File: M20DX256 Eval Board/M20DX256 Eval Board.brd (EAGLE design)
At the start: 60 x 30 mm, 20 parts, among them J1 M52-040000S0545, J2 20_PIN, J3 20_PIN, SW1 KMR211G, U1 MK20DX256VLH7, Y1 8MHz, Y2 32.768kHz, 12.5pF

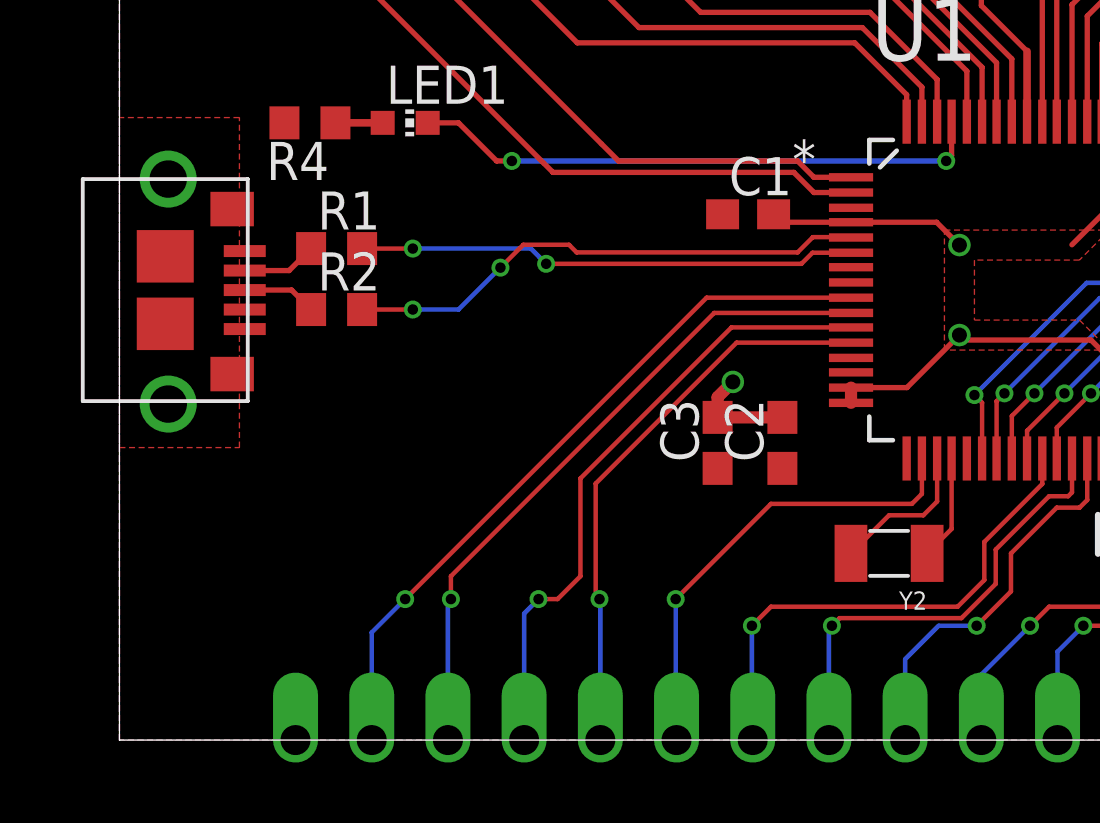
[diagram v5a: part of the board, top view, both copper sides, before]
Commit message: Add LED power to the schematic and route the board
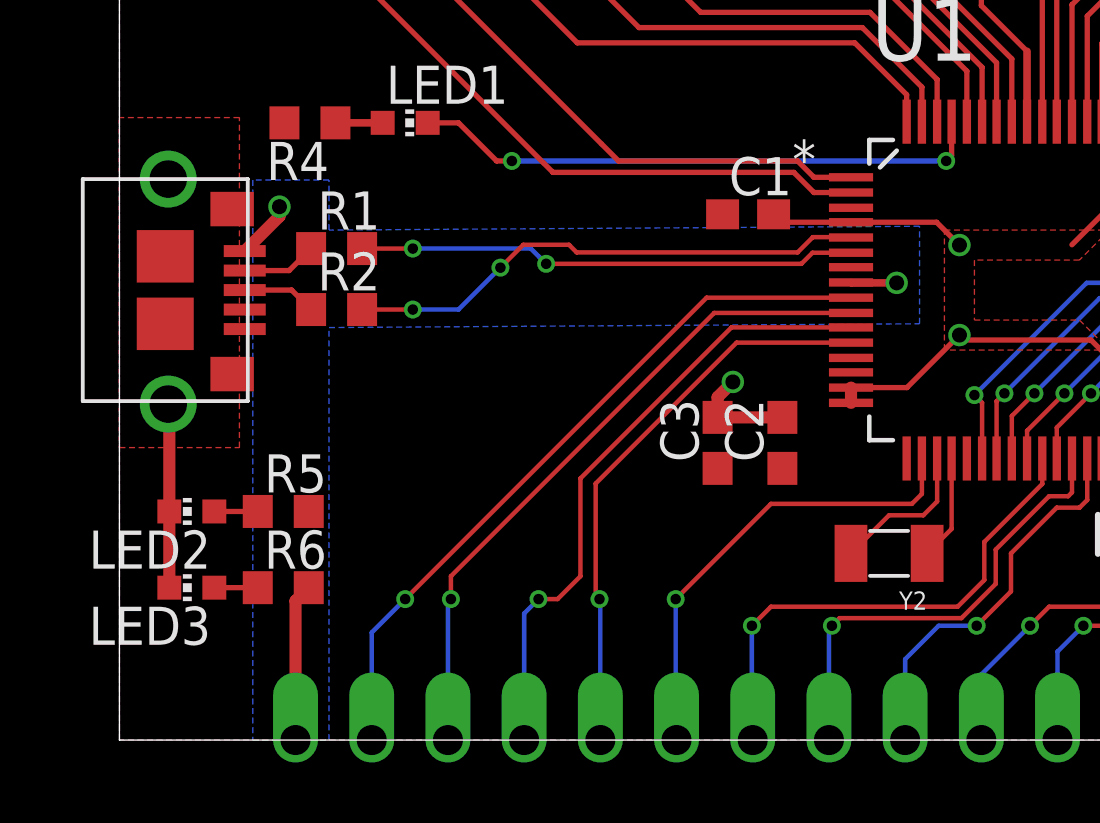
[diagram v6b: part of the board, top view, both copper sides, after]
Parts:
- added LED2, LED3: (no value), led:CHIP-LED0603
- added R5: 1k, rcl:R0603
- added R6: 1k5, rcl:R0603
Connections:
- new net N$10: LED2.A, R5.1
- new net N$9: LED3.A, R6.1
- net +3V3: now also R5.2
- net +5V: now also R6.2
- net GND: now also LED2.C, LED3.C
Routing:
- net +5V: track 0.00 -> 8.75 mm, vias 0 -> 2
- net GND: track 38.6 -> 44.8 mm
- net N$9: track 0.00 -> 1.45 mm
- net N$10: track 0.00 -> 1.45 mm
- added copper zone on layer 16, net +5V
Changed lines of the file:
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@@
 <element name="LED1" library="led" package="CHIP-LED0603" value="" x="9.525" y="20.574" rot="R270"/>
 <element name="R4" library="rcl" package="R0603" value="1k" x="6.35" y="20.574" rot="R180"/>
+<element name="R5" library="rcl" package="R0603" value="1k" x="5.461" y="7.62"/>
+<element name="R6" library="rcl" package="R0603" value="1k5" x="5.461" y="5.08"/>
+<element name="LED2" library="led" package="CHIP-LED0603" value="" x="2.413" y="7.62" rot="R90"/>
+<element name="LED3" library="led" package="CHIP-LED0603" value="" x="2.413" y="5.08" rot="R90"/>
 </elements>
 <signals>
@@
 <vertex x="0" y="0"/>
 </polygon>
+<contactref element="R5" pad="2"/>
 <wire x1="67.31" y1="26.25" x2="72.771" y2="26.123" width="0" layer="19" extent="1-1"/>
 <wire x1="57.035" y1="21.35" x2="67.31" y2="26.25" width="0" layer="19" extent="1-1"/>
@@
 <contactref element="SW1" pad="1"/>
 <contactref element="Y1" pad="2"/>
-<polygon width="0.4064" layer="16">
+<polygon width="0.4064" layer="16" rank="3">
 <vertex x="0" y="30"/>
 <vertex x="60" y="30"/>
@@
 <wire x1="37.6432" y1="18.2512" x2="38.227" y2="18.835" width="0.1778" layer="1"/>
 <contactref element="J3" pad="P$20"/>
+<contactref element="LED2" pad="C"/>
+<contactref element="LED3" pad="C"/>
+<wire x1="1.663" y1="5.08" x2="1.663" y2="7.62" width="0.4064" layer="1"/>
+<wire x1="1.663" y1="7.62" x2="1.663" y2="11.164" width="0.4064" layer="1"/>
+<wire x1="1.663" y1="11.164" x2="1.627" y2="11.2" width="0.4064" layer="1"/>
 <wire x1="67.31" y1="24.55" x2="72.771" y2="24.423" width="0" layer="19" extent="1-1"/>
 <wire x1="57.035" y1="20.08" x2="67.31" y2="24.55" width="0" layer="19" extent="1-1"/>
-<wire x1="54.13" y1="30" x2="57.035" y2="20.08" width="0" layer="19" extent="1-1"/>
 </signal>
 <signal name="+5V">
@@
 <contactref element="U1" pad="8"/>
 <contactref element="J2" pad="P$20"/>
-<wire x1="4.177" y1="16.3" x2="24.3866" y2="15.254" width="0" layer="19" extent="1-1"/>
-<wire x1="5.87" y1="0" x2="4.177" y2="16.3" width="0" layer="19" extent="1-1"/>
+<polygon width="0.1778" layer="16" spacing="0.254">
+<vertex x="4.445" y="0"/>
+<vertex x="6.985" y="0"/>
+<vertex x="6.985" y="13.75"/>
+<vertex x="26.67" y="13.877"/>
+<vertex x="26.67" y="17.127"/>
+<vertex x="6.985" y="17"/>
+<vertex x="6.985" y="18.669"/>
+<vertex x="4.445" y="18.669"/>
+</polygon>
+<wire x1="4.177" y1="16.3" x2="5.334" y2="17.457" width="0.4064" layer="1"/>
+<wire x1="5.334" y1="17.457" x2="5.334" y2="17.78" width="0.4064" layer="1"/>
+<via x="5.334" y="17.78" extent="1-16" drill="0.5"/>
+<wire x1="24.3866" y1="15.254" x2="24.4006" y2="15.24" width="0.254" layer="1"/>
+<wire x1="24.4006" y1="15.24" x2="25.908" y2="15.24" width="0.254" layer="1"/>
+<via x="25.908" y="15.24" extent="1-16" drill="0.5"/>
+<contactref element="R6" pad="2"/>
+<wire x1="5.87" y1="0" x2="5.87" y2="4.639" width="0.4064" layer="1"/>
+<wire x1="5.87" y1="4.639" x2="6.311" y2="5.08" width="0.4064" layer="1"/>
 </signal>
 <signal name="N$1">
@@
 <wire x1="18.542" y1="0.028" x2="18.57" y2="0" width="0.15" layer="16"/>
 </signal>
+<signal name="N$9">
+<contactref element="LED3" pad="A"/>
+<contactref element="R6" pad="1"/>
+<wire x1="4.611" y1="5.08" x2="3.163" y2="5.08" width="0.1778" layer="1"/>
+</signal>
+<signal name="N$10">
+<contactref element="LED2" pad="A"/>
+<contactref element="R5" pad="1"/>
+<wire x1="4.611" y1="7.62" x2="3.163" y2="7.62" width="0.1778" layer="1"/>
+</signal>
 </signals>

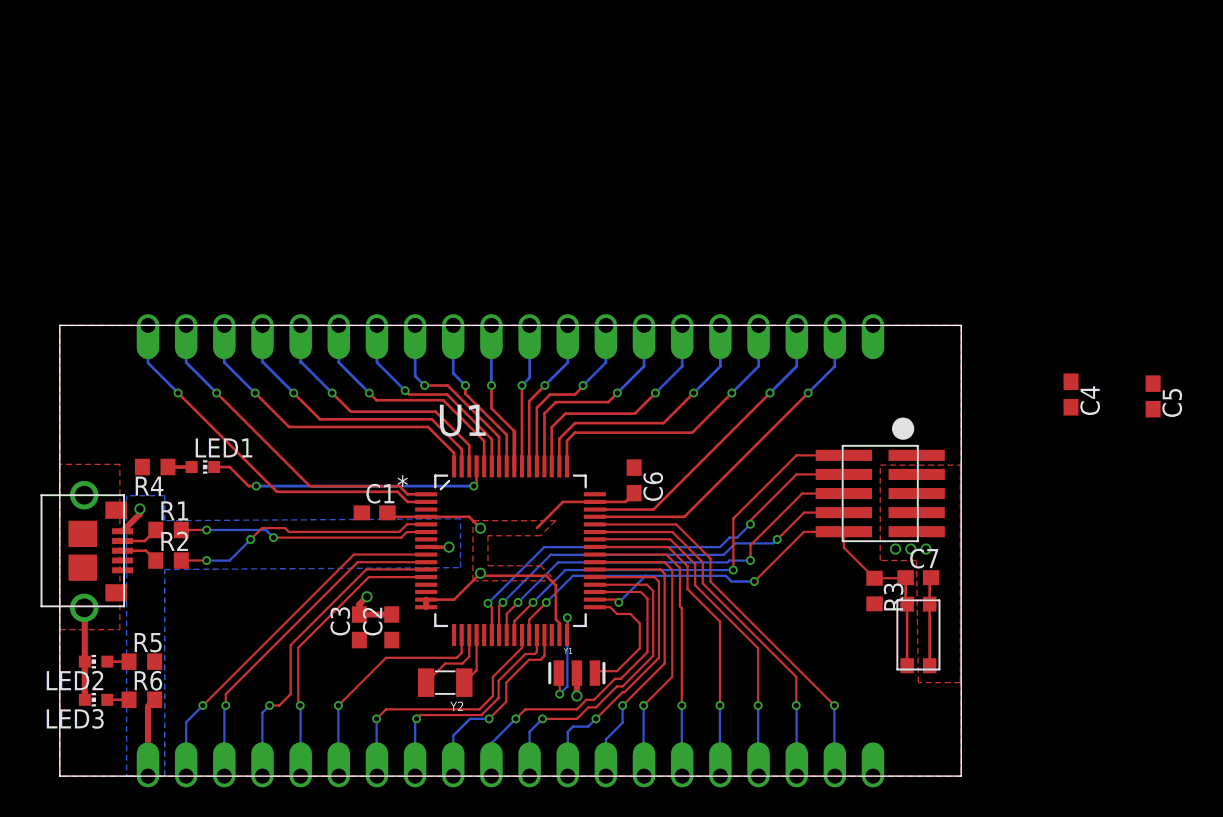
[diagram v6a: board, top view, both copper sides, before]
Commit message: Add test pad and curve the corner of the board
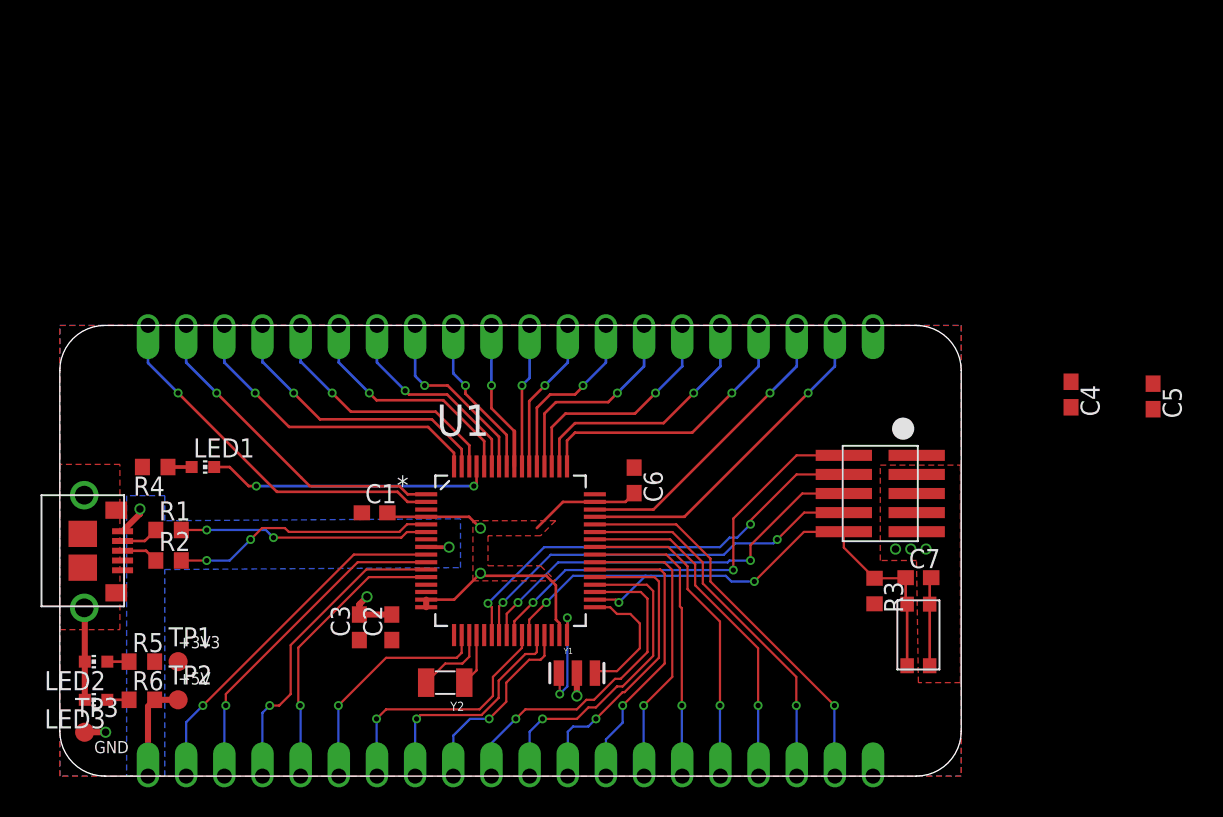
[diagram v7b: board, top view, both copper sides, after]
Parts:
- added TP1, TP2, TP3: TPB1,27, testpad:B1,27
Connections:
- net +3V3: now also TP1.TP
- net +5V: now also TP2.TP
- net GND: now also TP3.TP
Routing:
- net +5V: track 8.75 -> 10.3 mm
- net GND: track 44.8 -> 46.2 mm, vias 7 -> 8
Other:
- outline, holes or cut-outs redrawn
- board text added: "+3V3"
- board text added: "+5V"
- board text added: "GND"
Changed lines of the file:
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@@
 <layer number="46" name="Milling" color="3" fill="1" visible="no" active="yes"/>
 <layer number="47" name="Measures" color="7" fill="1" visible="no" active="yes"/>
-<layer number="48" name="Document" color="7" fill="1" visible="no" active="yes"/>
+<layer number="48" name="Document" color="7" fill="1" visible="yes" active="yes"/>
 <layer number="49" name="Reference" color="7" fill="1" visible="no" active="yes"/>
 <layer number="50" name="dxf" color="7" fill="1" visible="no" active="no"/>
@@
 <board>
 <plain>
-<wire x1="0" y1="0" x2="60" y2="0" width="0" layer="20"/>
-<wire x1="60" y1="0" x2="60" y2="30" width="0" layer="20"/>
-<wire x1="60" y1="30" x2="0" y2="30" width="0" layer="20"/>
-<wire x1="0" y1="30" x2="0" y2="0" width="0" layer="20"/>
+<wire x1="57" y1="30" x2="3" y2="30" width="0" layer="20"/>
+<wire x1="3" y1="30" x2="0" y2="27" width="0" layer="20" curve="90"/>
+<wire x1="0" y1="27" x2="0" y2="3" width="0" layer="20"/>
+<wire x1="0" y1="3" x2="3" y2="0" width="0" layer="20" curve="90"/>
+<wire x1="3" y1="0" x2="57" y2="0" width="0" layer="20"/>
+<wire x1="57" y1="0" x2="60" y2="3" width="0" layer="20" curve="90"/>
+<wire x1="60" y1="3" x2="60" y2="27" width="0" layer="20"/>
+<wire x1="60" y1="27" x2="57" y2="30" width="0" layer="20" curve="90"/>
+<text x="7.874" y="8.509" size="0.8128" layer="21">+3V3</text>
+<text x="7.874" y="6.096" size="0.8128" layer="21">+5V</text>
+<text x="2.286" y="1.524" size="0.8128" layer="21">GND</text>
 </plain>
 <attributes>
@@
 <element name="LED2" library="led" package="CHIP-LED0603" value="" x="2.413" y="7.62" rot="R90"/>
 <element name="LED3" library="led" package="CHIP-LED0603" value="" x="2.413" y="5.08" rot="R90"/>
+<element name="TP1" library="testpad" package="B1,27" value="TPB1,27" x="7.874" y="7.62">
+<attribute name="TP_SIGNAL_NAME" value="" x="7.874" y="7.62" size="1.778" layer="27" display="off"/>
+</element>
+<element name="TP2" library="testpad" package="B1,27" value="TPB1,27" x="7.874" y="5.08">
+<attribute name="TP_SIGNAL_NAME" value="" x="7.874" y="5.08" size="1.778" layer="27" display="off"/>
+</element>
+<element name="TP3" library="testpad" package="B1,27" value="TPB1,27" x="1.651" y="2.921">
+<attribute name="TP_SIGNAL_NAME" value="" x="1.651" y="2.921" size="0.8128" layer="27" display="off"/>
+</element>
 </elements>
 <signals>
@@
 </polygon>
 <contactref element="R5" pad="2"/>
+<contactref element="TP1" pad="TP"/>
 <wire x1="67.31" y1="26.25" x2="72.771" y2="26.123" width="0" layer="19" extent="1-1"/>
 <wire x1="57.035" y1="21.35" x2="67.31" y2="26.25" width="0" layer="19" extent="1-1"/>
@@
 <wire x1="1.663" y1="7.62" x2="1.663" y2="11.164" width="0.4064" layer="1"/>
 <wire x1="1.663" y1="11.164" x2="1.627" y2="11.2" width="0.4064" layer="1"/>
+<contactref element="TP3" pad="TP"/>
+<via x="3.048" y="2.921" extent="1-16" drill="0.5"/>
+<wire x1="1.651" y1="2.921" x2="3.048" y2="2.921" width="0.4064" layer="1"/>
 <wire x1="67.31" y1="24.55" x2="72.771" y2="24.423" width="0" layer="19" extent="1-1"/>
 <wire x1="57.035" y1="20.08" x2="67.31" y2="24.55" width="0" layer="19" extent="1-1"/>
@@
 <wire x1="5.87" y1="0" x2="5.87" y2="4.639" width="0.4064" layer="1"/>
 <wire x1="5.87" y1="4.639" x2="6.311" y2="5.08" width="0.4064" layer="1"/>
+<contactref element="TP2" pad="TP"/>
+<wire x1="6.311" y1="5.08" x2="7.874" y2="5.08" width="0.4064" layer="1"/>
 </signal>
 <signal name="N$1">

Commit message: Add fiducial
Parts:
- added JP1, JP2, JP3, JP4: FIDUCIAL1X2, SparkFun:FIDUCIAL-1X2
- moved LED2 0.89 mm to (2.41, 8.51)
- moved LED3 0.89 mm to (2.41, 5.97)
- moved R5 0.89 mm to (5.46, 8.51)
- moved R6 0.89 mm to (5.46, 5.97)
- moved TP1 0.89 mm to (7.87, 8.51)
- moved TP2 0.89 mm to (7.87, 5.97)
- moved TP3 0.89 mm to (1.65, 3.81)
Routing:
- net +5V: track 10.3 -> 11.2 mm
- net GND: track 46.2 -> 45.3 mm
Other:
- outline, holes or cut-outs redrawn
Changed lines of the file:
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@@
 <wire x1="57" y1="30" x2="3" y2="30" width="0" layer="20"/>
 <wire x1="3" y1="30" x2="0" y2="27" width="0" layer="20" curve="90"/>
-<wire x1="0" y1="27" x2="0" y2="3" width="0" layer="20"/>
-<wire x1="0" y1="3" x2="3" y2="0" width="0" layer="20" curve="90"/>
+<wire x1="0" y1="27" x2="0" y2="3.889" width="0" layer="20"/>
+<wire x1="0" y1="3.889" x2="3" y2="0" width="0" layer="20" curve="90"/>
 <wire x1="3" y1="0" x2="57" y2="0" width="0" layer="20"/>
 <wire x1="57" y1="0" x2="60" y2="3" width="0" layer="20" curve="90"/>
 <wire x1="60" y1="3" x2="60" y2="27" width="0" layer="20"/>
 <wire x1="60" y1="27" x2="57" y2="30" width="0" layer="20" curve="90"/>
-<text x="7.874" y="8.509" size="0.8128" layer="21">+3V3</text>
-<text x="7.874" y="6.096" size="0.8128" layer="21">+5V</text>
-<text x="2.286" y="1.524" size="0.8128" layer="21">GND</text>
+<text x="8.636" y="8.763" size="0.8128" layer="21">+3V3</text>
+<text x="8.636" y="6.223" size="0.8128" layer="21">+5V</text>
+<text x="3.683" y="3.556" size="0.8128" layer="21">GND</text>
 </plain>
 <attributes>
@@
 <element name="LED1" library="led" package="CHIP-LED0603" value="" x="9.525" y="20.574" rot="R270"/>
 <element name="R4" library="rcl" package="R0603" value="1k" x="6.35" y="20.574" rot="R180"/>
-<element name="R5" library="rcl" package="R0603" value="1k" x="5.461" y="7.62"/>
-<element name="R6" library="rcl" package="R0603" value="1k5" x="5.461" y="5.08"/>
-<element name="LED2" library="led" package="CHIP-LED0603" value="" x="2.413" y="7.62" rot="R90"/>
-<element name="LED3" library="led" package="CHIP-LED0603" value="" x="2.413" y="5.08" rot="R90"/>
-<element name="TP1" library="testpad" package="B1,27" value="TPB1,27" x="7.874" y="7.62">
-<attribute name="TP_SIGNAL_NAME" value="" x="7.874" y="7.62" size="1.778" layer="27" display="off"/>
+<element name="R5" library="rcl" package="R0603" value="1k" x="5.461" y="8.509"/>
+<element name="R6" library="rcl" package="R0603" value="1k5" x="5.461" y="5.969"/>
+<element name="LED2" library="led" package="CHIP-LED0603" value="" x="2.413" y="8.509" rot="R90"/>
+<element name="LED3" library="led" package="CHIP-LED0603" value="" x="2.413" y="5.969" rot="R90"/>
+<element name="TP1" library="testpad" package="B1,27" value="TPB1,27" x="7.874" y="8.509">
+<attribute name="TP_SIGNAL_NAME" value="" x="7.874" y="8.509" size="1.778" layer="27" display="off"/>
 </element>
-<element name="TP2" library="testpad" package="B1,27" value="TPB1,27" x="7.874" y="5.08">
-<attribute name="TP_SIGNAL_NAME" value="" x="7.874" y="5.08" size="1.778" layer="27" display="off"/>
+<element name="TP2" library="testpad" package="B1,27" value="TPB1,27" x="7.874" y="5.969">
+<attribute name="TP_SIGNAL_NAME" value="" x="7.874" y="5.969" size="1.778" layer="27" display="off"/>
 </element>
-<element name="TP3" library="testpad" package="B1,27" value="TPB1,27" x="1.651" y="2.921">
-<attribute name="TP_SIGNAL_NAME" value="" x="1.651" y="2.921" size="0.8128" layer="27" display="off"/>
+<element name="TP3" library="testpad" package="B1,27" value="TPB1,27" x="1.651" y="3.81">
+<attribute name="TP_SIGNAL_NAME" value="" x="1.651" y="3.81" size="0.8128" layer="27" display="off"/>
 </element>
+<element name="JP1" library="SparkFun" package="FIDUCIAL-1X2" value="FIDUCIAL1X2" x="2" y="2"/>
+<element name="JP2" library="SparkFun" package="FIDUCIAL-1X2" value="FIDUCIAL1X2" x="58" y="2"/>
+<element name="JP3" library="SparkFun" package="FIDUCIAL-1X2" value="FIDUCIAL1X2" x="2" y="28"/>
+<element name="JP4" library="SparkFun" package="FIDUCIAL-1X2" value="FIDUCIAL1X2" x="58" y="28"/>
 </elements>
 <signals>
@@
 <contactref element="LED2" pad="C"/>
 <contactref element="LED3" pad="C"/>
-<wire x1="1.663" y1="5.08" x2="1.663" y2="7.62" width="0.4064" layer="1"/>
-<wire x1="1.663" y1="7.62" x2="1.663" y2="11.164" width="0.4064" layer="1"/>
+<wire x1="1.663" y1="5.969" x2="1.663" y2="8.509" width="0.4064" layer="1"/>
+<wire x1="1.663" y1="8.509" x2="1.663" y2="11.164" width="0.4064" layer="1"/>
 <wire x1="1.663" y1="11.164" x2="1.627" y2="11.2" width="0.4064" layer="1"/>
 <contactref element="TP3" pad="TP"/>
-<via x="3.048" y="2.921" extent="1-16" drill="0.5"/>
-<wire x1="1.651" y1="2.921" x2="3.048" y2="2.921" width="0.4064" layer="1"/>
+<via x="3.048" y="3.81" extent="1-16" drill="0.5"/>
+<wire x1="1.651" y1="3.81" x2="3.048" y2="3.81" width="0.4064" layer="1"/>
 <wire x1="67.31" y1="24.55" x2="72.771" y2="24.423" width="0" layer="19" extent="1-1"/>
 <wire x1="57.035" y1="20.08" x2="67.31" y2="24.55" width="0" layer="19" extent="1-1"/>
@@
 <via x="25.908" y="15.24" extent="1-16" drill="0.5"/>
 <contactref element="R6" pad="2"/>
-<wire x1="5.87" y1="0" x2="5.87" y2="4.639" width="0.4064" layer="1"/>
-<wire x1="5.87" y1="4.639" x2="6.311" y2="5.08" width="0.4064" layer="1"/>
+<wire x1="5.87" y1="0" x2="5.87" y2="5.528" width="0.4064" layer="1"/>
+<wire x1="5.87" y1="5.528" x2="6.311" y2="5.969" width="0.4064" layer="1"/>
 <contactref element="TP2" pad="TP"/>
-<wire x1="6.311" y1="5.08" x2="7.874" y2="5.08" width="0.4064" layer="1"/>
+<wire x1="6.311" y1="5.969" x2="7.874" y2="5.969" width="0.4064" layer="1"/>
 </signal>
 <signal name="N$1">
@@
 <contactref element="LED3" pad="A"/>
 <contactref element="R6" pad="1"/>
-<wire x1="4.611" y1="5.08" x2="3.163" y2="5.08" width="0.1778" layer="1"/>
+<wire x1="4.611" y1="5.969" x2="3.163" y2="5.969" width="0.1778" layer="1"/>
 </signal>
 <signal name="N$10">
 <contactref element="LED2" pad="A"/>
 <contactref element="R5" pad="1"/>
-<wire x1="4.611" y1="7.62" x2="3.163" y2="7.62" width="0.1778" layer="1"/>
+<wire x1="4.611" y1="8.509" x2="3.163" y2="8.509" width="0.1778" layer="1"/>
 </signal>
 </signals>
